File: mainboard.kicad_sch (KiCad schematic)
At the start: 5 parts, among them J1 Raspi Pi Zero 2W, J2 LCD, J3 Keyboard, J4 USB_C_Receptacle_USB2.0

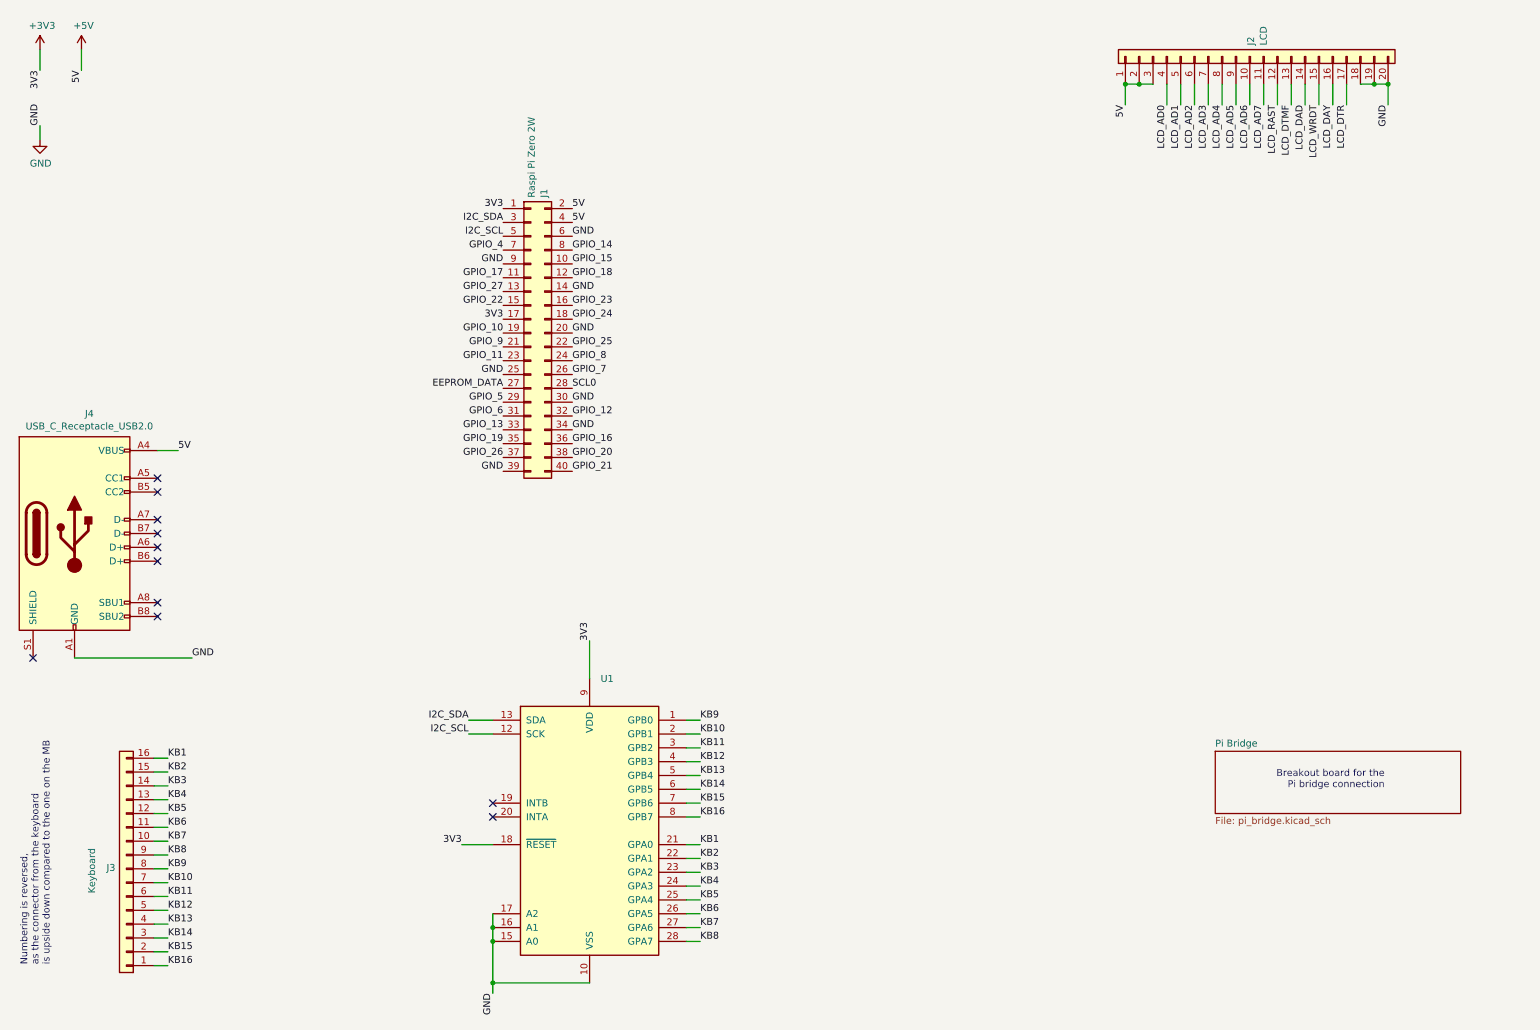
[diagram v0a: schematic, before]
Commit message: adding logic converter and power supply
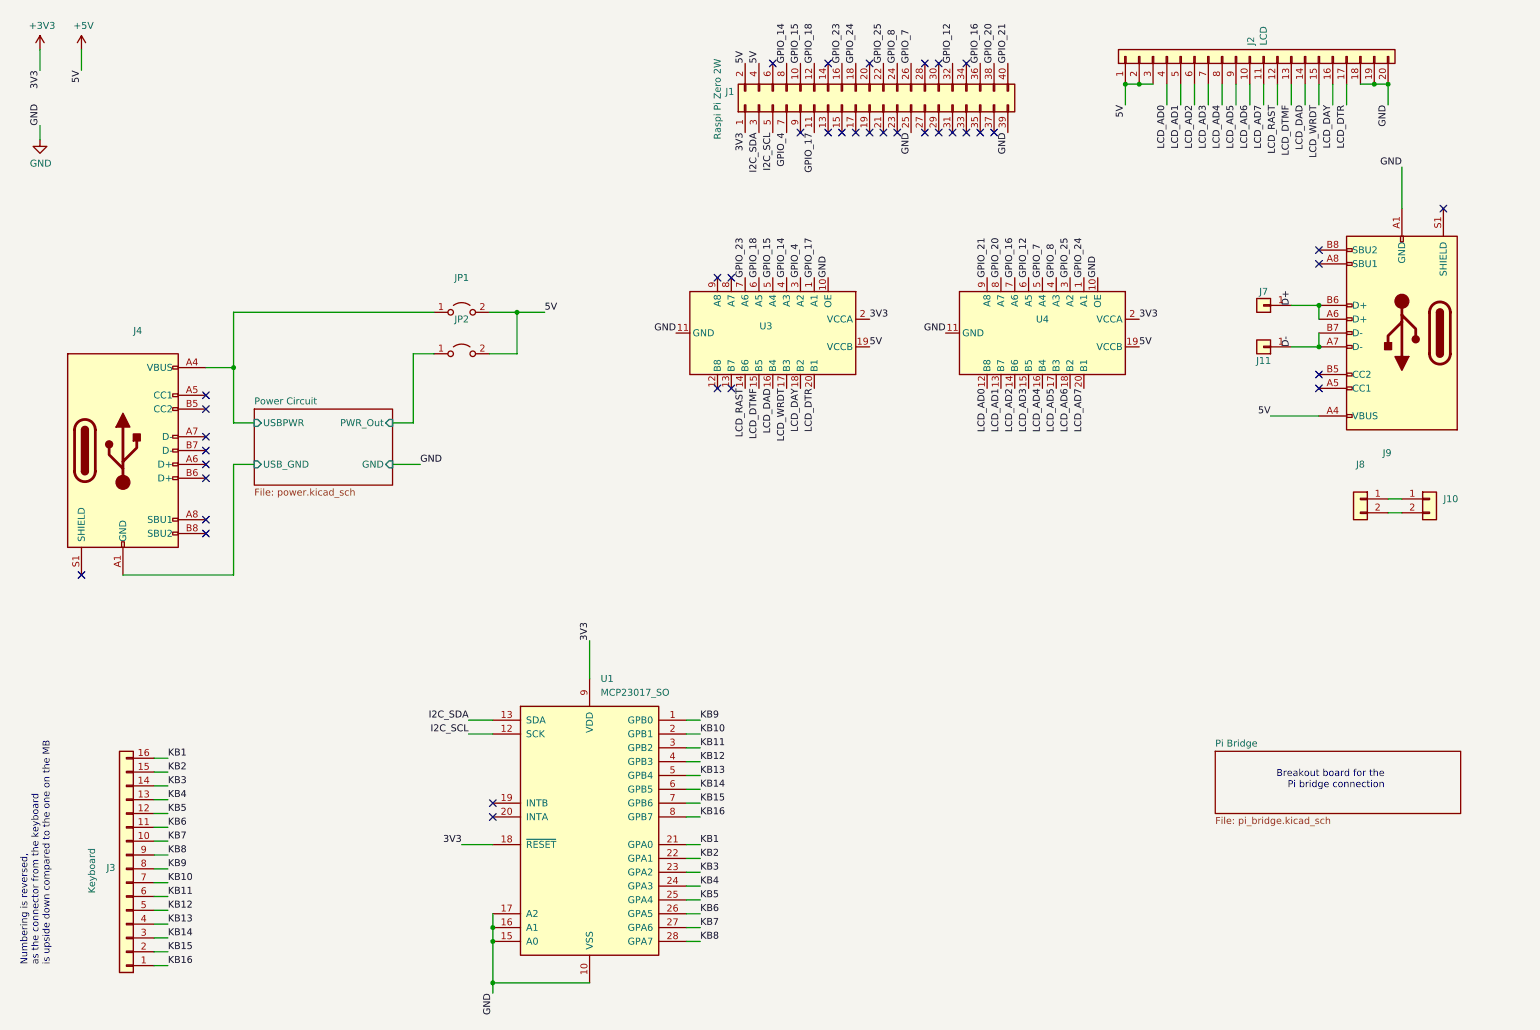
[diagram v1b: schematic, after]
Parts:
- added J10, J8: (no value), symbol Connector_Generic:Conn_01x02
- added J11, J7: (no value), symbol Connector_Generic:Conn_01x01
- added J9: (no value), symbol mainboard-rescue:USB_C_Receptacle_USB2.0-Connector
- added JP1, JP2: (no value), symbol Jumper:Jumper_2_Open
- added U3, U4: (no value), symbol Logic_LevelTranslator:TXS0108EPW
- J4: value USB_C_Receptacle_USB2.0 -> (none)
- U1: value (none) -> MCP23017_SO; footprint (none) -> Package_SO:SOIC-28W_7.5x17.9mm_P1.27mm
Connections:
- net +3V3: now also U3.2 (VCCA), U4.2 (VCCA); no longer J1.17 (Pin_17)
- net +5V: now also J9.A4 (VBUS), J9.A9 (VBUS), J9.B4 (VBUS), J9.B9 (VBUS), JP1.2 (B), JP2.2 (B), U3.19 (VCCB), U4.19 (VCCB); no longer J4.A4 (VBUS), J4.A9 (VBUS), J4.B4 (VBUS), J4.B9 (VBUS)
- net GND: now also J9.A1 (GND), J9.A12 (GND), J9.B1 (GND), J9.B12 (GND), U3.10 (OE), U3.11 (GND), U4.10 (OE), U4.11 (GND); no longer J1.14 (Pin_14), J1.20 (Pin_20), J1.30 (Pin_30), J1.34 (Pin_34), J1.6 (Pin_6), J1.9 (Pin_9), J4.A1 (GND), J4.A12 (GND), J4.B1 (GND), J4.B12 (GND)
- net GPIO_12: now also U4.6 (A5)
- net GPIO_14: now also U3.4 (A3)
- net GPIO_15: now also U3.5 (A4)
- net GPIO_16: now also U4.7 (A6)
- net GPIO_17: now also U3.1 (A1)
- net GPIO_18: now also U3.6 (A5)
- net GPIO_20: now also U4.8 (A7)
- net GPIO_21: now also U4.9 (A8)
- net GPIO_23: now also U3.7 (A6)
- net GPIO_24: now also U4.1 (A1)
- net GPIO_25: now also U4.3 (A2)
- net GPIO_4: now also U3.3 (A2)
- net GPIO_7: now also U4.5 (A4)
- net GPIO_8: now also U4.4 (A3)
- net LCD_AD0: now also U4.12 (B8)
- net LCD_AD1: now also U4.13 (B7)
- net LCD_AD2: now also U4.14 (B6)
- net LCD_AD3: now also U4.15 (B5)
- net LCD_AD4: now also U4.16 (B4)
- net LCD_AD5: now also U4.17 (B3)
- net LCD_AD6: now also U4.18 (B2)
- net LCD_AD7: now also U4.20 (B1)
- net LCD_DAD: now also U3.16 (B4)
- net LCD_DAY: now also U3.18 (B2)
- net LCD_DTMF: now also U3.15 (B5)
- net LCD_DTR: now also U3.20 (B1)
- net LCD_RAST: now also U3.14 (B6)
- net LCD_WRDT: now also U3.17 (B3)
- net EEPROM_DATA: no longer names the net of J1.27 (Pin_27)
- net GPIO_10: no longer names the net of J1.19 (Pin_19)
- net GPIO_11: no longer names the net of J1.23 (Pin_23)
- net GPIO_13: no longer names the net of J1.33 (Pin_33)
- net GPIO_19: no longer names the net of J1.35 (Pin_35)
- net GPIO_22: no longer names the net of J1.15 (Pin_15)
- net GPIO_26: no longer names the net of J1.37 (Pin_37)
- net GPIO_27: no longer names the net of J1.13 (Pin_13)
- net GPIO_5: no longer names the net of J1.29 (Pin_29)
- net GPIO_6: no longer names the net of J1.31 (Pin_31)
- net GPIO_9: no longer names the net of J1.21 (Pin_21)
- net SCL0: no longer names the net of J1.28 (Pin_28)
- new net: J10.1 (Pin_1), J8.1 (Pin_1)
- new net: J10.2 (Pin_2), J8.2 (Pin_2)
- new net D+: J7.1 (Pin_1), J9.A6 (D+), J9.B6 (D+)
- new net D-: J11.1 (Pin_1), J9.A7 (D-), J9.B7 (D-)
- new net Power Circuit/PWR_Out: JP2.1 (A)
- new net Power Circuit/USBPWR: J4.A4 (VBUS), J4.A9 (VBUS), J4.B4 (VBUS), J4.B9 (VBUS), JP1.1 (A)
- new net Power Circuit/USB_GND: J4.A1 (GND), J4.A12 (GND), J4.B1 (GND), J4.B12 (GND)
- no-connect marks 11 -> 39
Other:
- added sheet Power Circuit (power.kicad_sch)
- moved on the sheet: J1

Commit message: Adding switch to power
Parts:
- added SW1: (no value), symbol Switch:SW_SPST
- J10: value (none) -> USBDataBoard; footprint (none) -> Connector_PinHeader_2.00mm:PinHeader_1x02_P2.00mm_Vertical
- J11: value (none) -> DM; footprint (none) -> TestPoint:TestPoint_Pad_D1.0mm
- J4: value (none) -> USB Power; footprint (none) -> Connector_USB:USB_C_Receptacle_XKB_U262-16XN-4BVC11
- J7: value (none) -> DP; footprint (none) -> TestPoint:TestPoint_Pad_D1.0mm
- J8: value (none) -> USBDataPi; footprint (none) -> Connector_PinHeader_2.00mm:PinHeader_1x02_P2.00mm_Vertical
- J9: value (none) -> USB Data; footprint (none) -> Connector_USB:USB_C_Receptacle_XKB_U262-16XN-4BVC11
- JP1: value (none) -> JMP_USB; footprint (none) -> Jumper:SolderJumper-2_P1.3mm_Open_RoundedPad1.0x1.5mm
- JP2: value (none) -> JMP_BAT; footprint (none) -> Jumper:SolderJumper-2_P1.3mm_Open_RoundedPad1.0x1.5mm
- U3, U4: value (none) -> TXS0108EPW; footprint (none) -> Package_SO:TSSOP-20_4.4x6.5mm_P0.65mm
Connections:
- net +5V: now also SW1.2 (B); no longer JP1.2 (B), JP2.2 (B)
- new net: JP1.2 (B), JP2.2 (B), SW1.1 (A)
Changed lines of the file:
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@@
+    (stroke (width 0) (type default) (color 0 0 0 0))
+  )
+  (wire (pts (xy 121.92 67.31) (xy 124.46 67.31))
     (stroke (width 0) (type default) (color 0 0 0 0))
   )
@@
     (effects (font (size 1.27 1.27)) (justify right bottom))
   )
-  (label "5V" (at 111.76 67.31 0)
+  (label "5V" (at 124.46 67.31 0)
     (effects (font (size 1.27 1.27)) (justify left bottom))
   )
@@
     (in_bom yes) (on_board yes)
     (property "Reference" "J7" (id 0) (at 243.84 63.5 0))
-    (property "Value" "" (id 1) (at 240.03 66.04 0))
-    (property "Footprint" "" (id 2) (at 243.84 66.04 0)
+    (property "Value" "DP" (id 1) (at 240.03 66.04 0))
+    (property "Footprint" "TestPoint:TestPoint_Pad_D1.0mm" (id 2) (at 243.84 66.04 0)
       (effects (font (size 1.27 1.27)) hide)
     )
@@
     (in_bom yes) (on_board yes)
     (property "Reference" "J11" (id 0) (at 243.84 76.2 0))
-    (property "Value" "" (id 1) (at 240.03 73.66 0))
-    (property "Footprint" "" (id 2) (at 243.84 73.66 0)
+    (property "Value" "DM" (id 1) (at 240.03 73.66 0))
+    (property "Footprint" "TestPoint:TestPoint_Pad_D1.0mm" (id 2) (at 243.84 73.66 0)
       (effects (font (size 1.27 1.27)) hide)
     )
@@
       (effects (font (size 1.27 1.27)) (justify left))
     )
-    (property "Value" "" (id 1) (at 276.86 104.1399 0)
-      (effects (font (size 1.27 1.27)) (justify left))
-    )
-    (property "Footprint" "" (id 2) (at 274.32 101.6 0)
+    (property "Value" "USBDataBoard" (id 1) (at 276.86 104.1399 0)
+      (effects (font (size 1.27 1.27)) (justify left))
+    )
+    (property "Footprint" "Connector_PinHeader_2.00mm:PinHeader_1x02_P2.00mm_Vertical" (id 2) (at 274.32 101.6 0)
       (effects (font (size 1.27 1.27)) hide)
     )
@@
     (in_bom yes) (on_board yes)
     (property "Reference" "U4" (id 0) (at 203.2 68.58 90))
-    (property "Value" "" (id 1) (at 203.2 72.39 90))
-    (property "Footprint" "" (id 2) (at 184.15 71.12 0)
+    (property "Value" "TXS0108EPW" (id 1) (at 203.2 72.39 90))
+    (property "Footprint" "Package_SO:TSSOP-20_4.4x6.5mm_P0.65mm" (id 2) (at 184.15 71.12 0)
       (effects (font (size 1.27 1.27)) hide)
     )
@@
     (in_bom yes) (on_board yes) (fields_autoplaced)
     (property "Reference" "J8" (id 0) (at 261.62 95.25 0))
-    (property "Value" "" (id 1) (at 261.62 97.79 0))
-    (property "Footprint" "" (id 2) (at 261.62 101.6 0)
+    (property "Value" "USBDataPi" (id 1) (at 261.62 97.79 0))
+    (property "Footprint" "Connector_PinHeader_2.00mm:PinHeader_1x02_P2.00mm_Vertical" (id 2) (at 261.62 101.6 0)
       (effects (font (size 1.27 1.27)) hide)
     )
@@
     (in_bom yes) (on_board yes)
     (property "Reference" "J4" (id 0) (at 37.0078 70.6882 0))
-    (property "Value" "" (id 1) (at 37.0078 72.9996 0))
-    (property "Footprint" "" (id 2) (at 38.1 92.71 0)
+    (property "Value" "USB Power" (id 1) (at 37.0078 72.9996 0))
+    (property "Footprint" "Connector_USB:USB_C_Receptacle_XKB_U262-16XN-4BVC11" (id 2) (at 38.1 92.71 0)
       (effects (font (size 1.27 1.27)) hide)
     )
@@
     (pin "S1")
   )
+  (symbol (lib_id "Switch:SW_SPST") (at 116.84 67.31 0) (unit 1)
+    (in_bom yes) (on_board yes) (fields_autoplaced)
+    (property "Reference" "SW1" (id 0) (at 116.84 60.96 0))
+    (property "Value" "" (id 1) (at 116.84 63.5 0))
+    (property "Footprint" "" (id 2) (at 116.84 67.31 0)
+      (effects (font (size 1.27 1.27)) hide)
+    )
+    (property "Datasheet" "~" (id 3) (at 116.84 67.31 0)
+      (effects (font (size 1.27 1.27)) hide)
+    )
+    (pin "1")
+    (pin "2")
+  )
   (symbol (lib_id "Jumper:Jumper_2_Open") (at 96.52 67.31 0) (unit 1)
     (in_bom yes) (on_board yes) (fields_autoplaced)
     (property "Reference" "JP1" (id 0) (at 96.52 60.96 0))
-    (property "Value" "" (id 1) (at 96.52 63.5 0))
-    (property "Footprint" "" (id 2) (at 96.52 67.31 0)
+    (property "Value" "JMP_USB" (id 1) (at 96.52 63.5 0))
+    (property "Footprint" "Jumper:SolderJumper-2_P1.3mm_Open_RoundedPad1.0x1.5mm" (id 2) (at 96.52 67.31 0)
       (effects (font (size 1.27 1.27)) hide)
     )
@@
     (in_bom yes) (on_board yes)
     (property "Reference" "U3" (id 0) (at 152.4 69.85 90))
-    (property "Value" "" (id 1) (at 153.67 73.66 90))
-    (property "Footprint" "" (id 2) (at 134.62 71.12 0)
+    (property "Value" "TXS0108EPW" (id 1) (at 153.67 73.66 90))
+    (property "Footprint" "Package_SO:TSSOP-20_4.4x6.5mm_P0.65mm" (id 2) (at 134.62 71.12 0)
       (effects (font (size 1.27 1.27)) hide)
     )
@@
     (in_bom yes) (on_board yes) (fields_autoplaced)
     (property "Reference" "JP2" (id 0) (at 96.52 68.58 0))
-    (property "Value" "" (id 1) (at 96.52 71.12 0))
-    (property "Footprint" "" (id 2) (at 96.52 74.93 0)
+    (property "Value" "JMP_BAT" (id 1) (at 96.52 71.12 0))
+    (property "Footprint" "Jumper:SolderJumper-2_P1.3mm_Open_RoundedPad1.0x1.5mm" (id 2) (at 96.52 74.93 0)
       (effects (font (size 1.27 1.27)) hide)
     )
@@
     (in_bom yes) (on_board yes)
     (property "Reference" "J9" (id 0) (at 266.5222 93.1418 0))
-    (property "Value" "" (id 1) (at 266.5222 90.8304 0))
-    (property "Footprint" "" (id 2) (at 265.43 71.12 0)
+    (property "Value" "USB Data" (id 1) (at 266.5222 90.8304 0))
+    (property "Footprint" "Connector_USB:USB_C_Receptacle_XKB_U262-16XN-4BVC11" (id 2) (at 265.43 71.12 0)
       (effects (font (size 1.27 1.27)) hide)
     )
@@
       (reference "R3") (unit 1) (value "10k") (footprint "Resistor_SMD:R_0805_2012Metric_Pad1.20x1.40mm_HandSolder")
     )
+    (path "/82771776-27f6-4c8a-8652-f67ca7a2b4f5"
+      (reference "SW1") (unit 1) (value "SW_SPST") (footprint "Library:SS312SAH4-R")
+    )
     (path "/1feae217-1d71-4844-9474-f37767f13e6c"

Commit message: v0.2
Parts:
- added R4, R5: 5.1k, Resistor_SMD:R_0805_2012Metric_Pad1.20x1.40mm_HandSolder, symbol Device:R
- SW1: value (none) -> SW_SPST; footprint (none) -> Library:SS312SAH4-R
- U1: footprint Package_SO:SOIC-28W_7.5x17.9mm_P1.27mm -> Package_SO:TSSOP-28_8x9.7mm_P0.65mm
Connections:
- net +3V3: now also U3.10 (OE), U4.10 (OE)
- net GND: no longer U3.10 (OE), U4.10 (OE)
- net Power Circuit/USB_GND: now also R4.2, R5.2
- net at J4.A5 (CC1): now also R5.1
- net at J4.B5 (CC2): now also R4.1
- no-connect marks 39 -> 37
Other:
- moved on the sheet: JP1, JP2

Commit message: updating footprint
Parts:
- U1: footprint Package_SO:TSSOP-28_8x9.7mm_P0.65mm -> Package_SO:TSSOP-28_6.1x9.7mm_P0.65mm
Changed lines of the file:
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@@
       (effects (font (size 1.27 1.27)) (justify left))
     )
-    (property "Footprint" "Package_SO:TSSOP-28_8x9.7mm_P0.65mm" (id 2) (at 125.095 187.96 0)
+    (property "Footprint" "Package_SO:TSSOP-28_6.1x9.7mm_P0.65mm" (id 2) (at 125.095 187.96 0)
       (effects (font (size 1.27 1.27)) (justify left) hide)
     )
@@
     )
     (path "/1feae217-1d71-4844-9474-f37767f13e6c"
-      (reference "U1") (unit 1) (value "MCP23017_SO") (footprint "Package_SO:TSSOP-28_8x9.7mm_P0.65mm")
+      (reference "U1") (unit 1) (value "MCP23017_SO") (footprint "Package_SO:TSSOP-28_6.1x9.7mm_P0.65mm")
     )
     (path "/dc813488-eaf9-49a2-8951-d7d91abb4600/1c21c6f5-3e71-4be3-bf45-d619c41235dc"
